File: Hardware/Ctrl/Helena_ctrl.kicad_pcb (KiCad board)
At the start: 2 copper layers, 38 x 18 mm, 41 parts, among them P1 CONN_01X06, P2 CONN_01X04, Q1 BC857C, SW1 SW_PUSH, U1 antenna-gnd, U2 nrf51822-qfax, U3 MPU-6050, Y1 16MHz

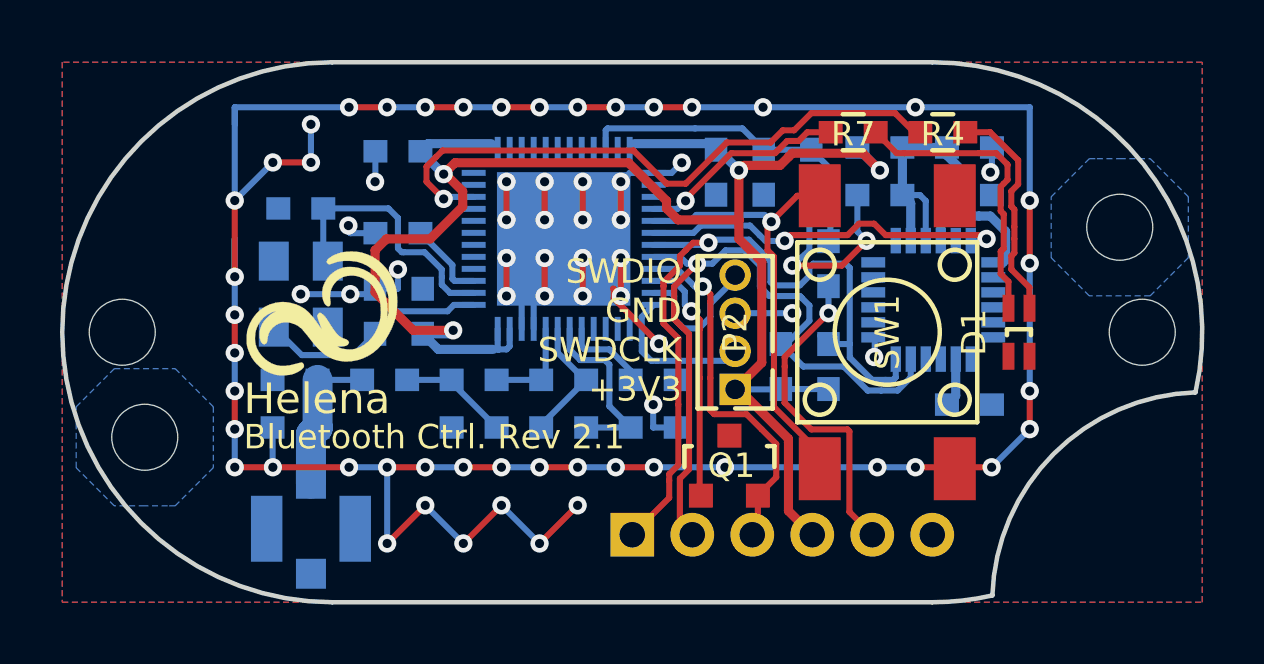
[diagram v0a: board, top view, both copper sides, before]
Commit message: added reverse polarity protection and led board
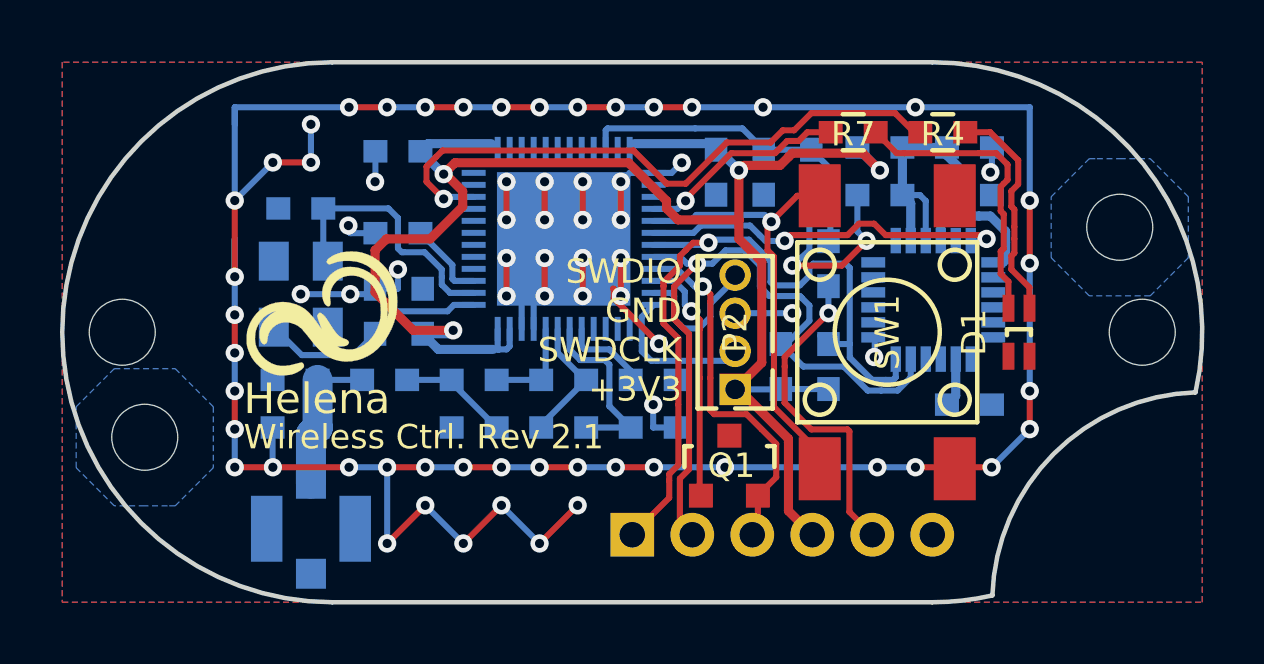
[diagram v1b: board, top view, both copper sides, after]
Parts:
- C1: value ? -> dnp
- C11: value 47n -> 100n
- R3, R5: value 3k3 -> 1k5
- R4: value 560 -> 680
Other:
- board text added: "Wireless Ctrl. Rev 2.1"
- board text removed: "Bluetooth Ctrl. Rev 2.1"
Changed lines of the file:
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@@
-(kicad_pcb (version 4) (host pcbnew 4.0.2-stable)
+(kicad_pcb (version 4) (host pcbnew 4.0.5)
   (general
     (links 107)
     (no_connects 0)
-    (area 23.415457 140.8631 76.584543 161.810733)
+    (area 30.924999 140.924999 69.075001 159.075001)
     (thickness 1.6)
     (drawings 23)
@@
   )
   (page A4)
+  (title_block
+    (title "Helena Wireless Control Board")
+    (date 2016-12-15)
+    (rev 2.1)
+  )
   (layers
-    (0 F.Cu signal hide)
-    (31 B.Cu signal)
+    (0 F.Cu signal)
+    (31 B.Cu signal hide)
     (32 B.Adhes user hide)
     (33 F.Adhes user hide)
@@
     (35 F.Paste user)
     (36 B.SilkS user)
-    (37 F.SilkS user hide)
+    (37 F.SilkS user)
     (38 B.Mask user hide)
     (39 F.Mask user)
@@
     (aux_axis_origin 0 0)
     (grid_origin 50 150)
-    (visible_elements 7FFCBF7F)
+    (visible_elements 7FFC7F7F)
     (pcbplotparams
       (layerselection 0x00030_80000001)
@@
       (effects (font (size 0.8128 0.8128) (thickness 0.1524)) (justify mirror))
     )
-    (fp_text value ? (at 0 -1.9 180) (layer B.Fab)
+    (fp_text value dnp (at 0 -1.9 180) (layer B.Fab)
       (effects (font (size 1 1) (thickness 0.15)) (justify mirror))
     )
@@
       (effects (font (size 0.8128 0.8128) (thickness 0.1524)) (justify mirror))
     )
-    (fp_text value 47n (at 0 -1.9) (layer B.Fab)
+    (fp_text value 100n (at 0 -1.9) (layer B.Fab)
       (effects (font (size 1 1) (thickness 0.15)) (justify mirror))
     )
@@
       (effects (font (size 0.8128 0.8128) (thickness 0.1524)) (justify mirror))
     )
-    (fp_text value 3k3 (at 0 -1.9 90) (layer B.Fab)
+    (fp_text value 1k5 (at 0 -1.9 90) (layer B.Fab)
       (effects (font (size 1 1) (thickness 0.15)) (justify mirror))
     )
@@
       (effects (font (size 0.8128 0.8128) (thickness 0.1524)))
     )
-    (fp_text value 560 (at 0 1.9) (layer F.Fab)
+    (fp_text value 680 (at 0 1.9) (layer F.Fab)
       (effects (font (size 1 1) (thickness 0.15)))
     )
@@
       (effects (font (size 0.8128 0.8128) (thickness 0.1524)) (justify mirror))
     )
-    (fp_text value 3k3 (at 0 -1.9 90) (layer B.Fab)
+    (fp_text value 1k5 (at 0 -1.9 90) (layer B.Fab)
       (effects (font (size 1 1) (thickness 0.15)) (justify mirror))
     )
@@
     (effects (font (size 0.8128 0.8128) (thickness 0.1524)) (justify right))
   )
-  (gr_text "Bluetooth Ctrl. Rev 2.1" (at 37.046 153.4925) (layer F.SilkS)
+  (gr_text "Wireless Ctrl. Rev 2.1" (at 37.046 153.4925) (layer F.SilkS)
     (effects (font (size 0.8128 0.8128) (thickness 0.1524)) (justify left))
   )
